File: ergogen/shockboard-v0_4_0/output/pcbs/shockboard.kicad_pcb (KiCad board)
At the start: 2 copper layers, 282.9 x 126 mm, 159 parts

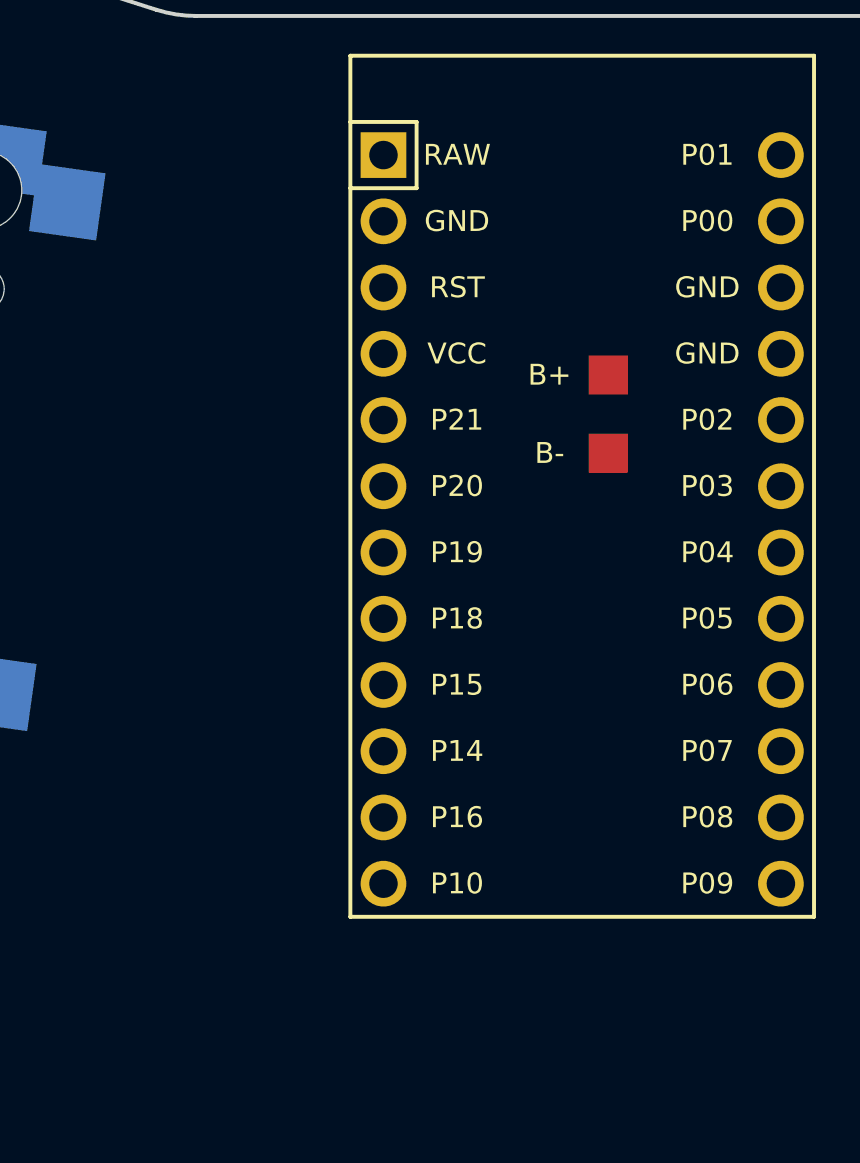
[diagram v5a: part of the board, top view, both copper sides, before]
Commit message: feat: added reset switch and oled
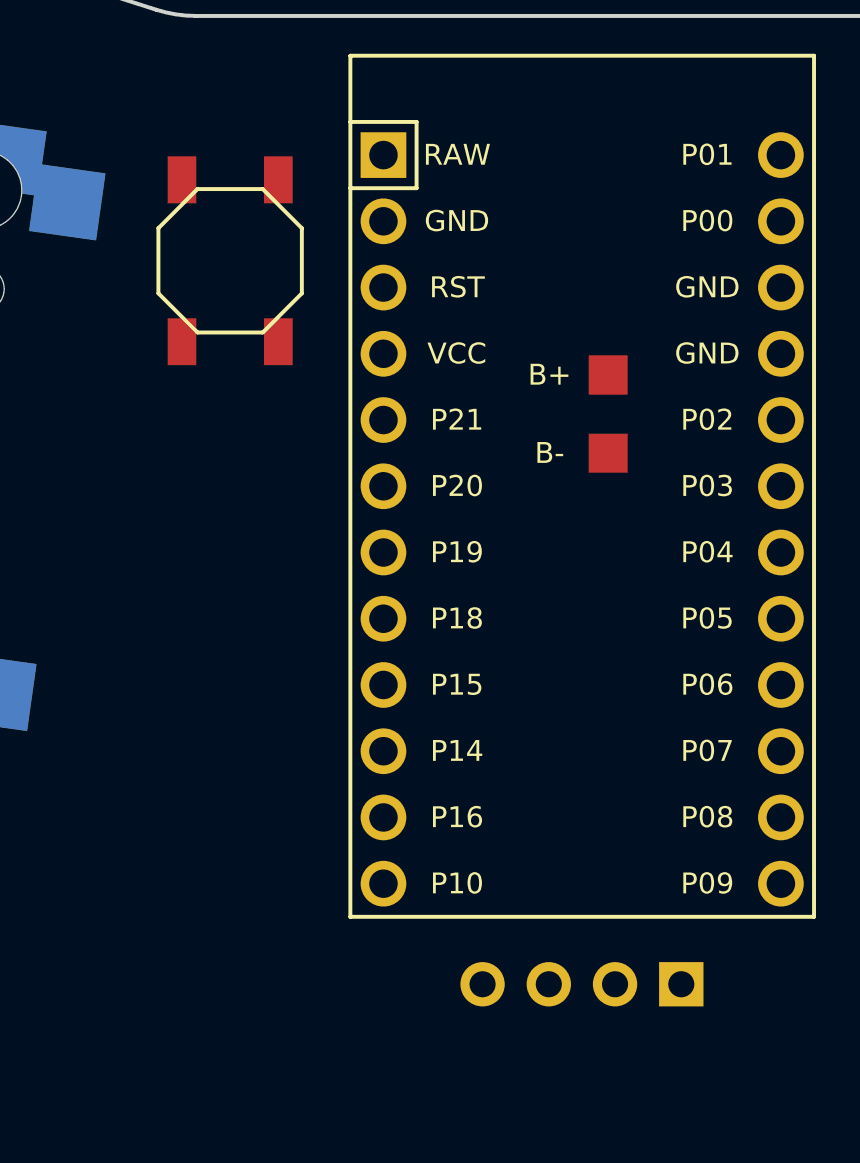
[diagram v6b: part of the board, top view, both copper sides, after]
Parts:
- added B1: , E73:SW_TACT_ALPS_SKQGABE010, F.Cu at (198.9, 92.2)
- added OLED1: OLED, lib:OLED_headers, F.Cu at (206.4, 121.5)
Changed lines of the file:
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@@
 (fp_text user B- (at -2.25 0 0) (layer F.SilkS) (effects (font (size 0.8 0.8) (thickness 0.15)) ))
         )
+        (module lib:OLED_headers (layer F.Cu)
+        (at 206.3782709 121.5245405 90)
+        (fp_text reference "OLED1" (at 0 0) (layer F.SilkS) hide (effects (font (size 1.27 1.27) (thickness 0.15))))
+        (fp_text value OLED (at 0 -7.3) (layer F.Fab) (effects (font (size 1 1) (thickness 0.15))))
+        (pad 4 thru_hole oval (at 1.6 2.18 360) (size 1.7 1.7) (drill 1) (layers *.Cu *.Mask)
+        (net 43 "P2"))
+        (pad 3 thru_hole oval (at 1.6 4.72 360) (size 1.7 1.7) (drill 1) (layers *.Cu *.Mask)
+        (net 48 "P3"))
+        (pad 2 thru_hole oval (at 1.6 7.26 360) (size 1.7 1.7) (drill 1) (layers *.Cu *.Mask)
+        (net 73 "VCC"))
+        (pad 1 thru_hole rect (at 1.6 9.8 360) (size 1.7 1.7) (drill 1) (layers *.Cu *.Mask)
+        (net 71 "GND"))
+        )
+    (module E73:SW_TACT_ALPS_SKQGABE010 (layer F.Cu)
+        (descr "Low-profile SMD Tactile Switch, https://www.e-switch.com/product-catalog/tact/product-lines/tl3342-series-low-profile-smt-tact-switch")
+        (tags "SPST Tactile Switch")
+        (at 198.87827089999996 92.1818495 90)
+        (fp_text reference "B1" (at 0 0) (layer F.SilkS) hide (effects (font (size 1.27 1.27) (thickness 0.15))))
+        (fp_text value "" (at 0 0) (layer F.SilkS) hide (effects (font (size 1.27 1.27) (thickness 0.15))))
+        (fp_line (start 2.75 1.25) (end 1.25 2.75) (layer F.SilkS) (width 0.15))
+        (fp_line (start 2.75 -1.25) (end 1.25 -2.75) (layer F.SilkS) (width 0.15))
+        (fp_line (start 2.75 -1.25) (end 2.75 1.25) (layer F.SilkS) (width 0.15))
+        (fp_line (start -1.25 2.75) (end 1.25 2.75) (layer F.SilkS) (width 0.15))
+        (fp_line (start -1.25 -2.75) (end 1.25 -2.75) (layer F.SilkS) (width 0.15))
+        (fp_line (start -2.75 1.25) (end -1.25 2.75) (layer F.SilkS) (width 0.15))
+        (fp_line (start -2.75 -1.25) (end -1.25 -2.75) (layer F.SilkS) (width 0.15))
+        (fp_line (start -2.75 -1.25) (end -2.75 1.25) (layer F.SilkS) (width 0.15))
+        (pad 1 smd rect (at -3.1 -1.85 90) (size 1.8 1.1) (layers F.Cu F.Paste F.Mask) (net 71 "GND"))
+        (pad 1 smd rect (at 3.1 -1.85 90) (size 1.8 1.1) (layers F.Cu F.Paste F.Mask) (net 71 "GND"))
+        (pad 2 smd rect (at -3.1 1.85 90) (size 1.8 1.1) (layers F.Cu F.Paste F.Mask) (net 72 "RST"))
+        (pad 2 smd rect (at 3.1 1.85 90) (size 1.8 1.1) (layers F.Cu F.Paste F.Mask) (net 72 "RST"))
+    )
             (gr_line (start 281.0227501060654 193.85241200000002) (end 143.73379169393456 193.85241200000002) (angle 90) (layer Edge.Cuts) (width 0.15))
 (gr_line (start 140.8586163541582 192.94305577204256) (end 87.51792705748205 155.4516883672485) (angle 90) (layer Edge.Cuts) (width 0.15))

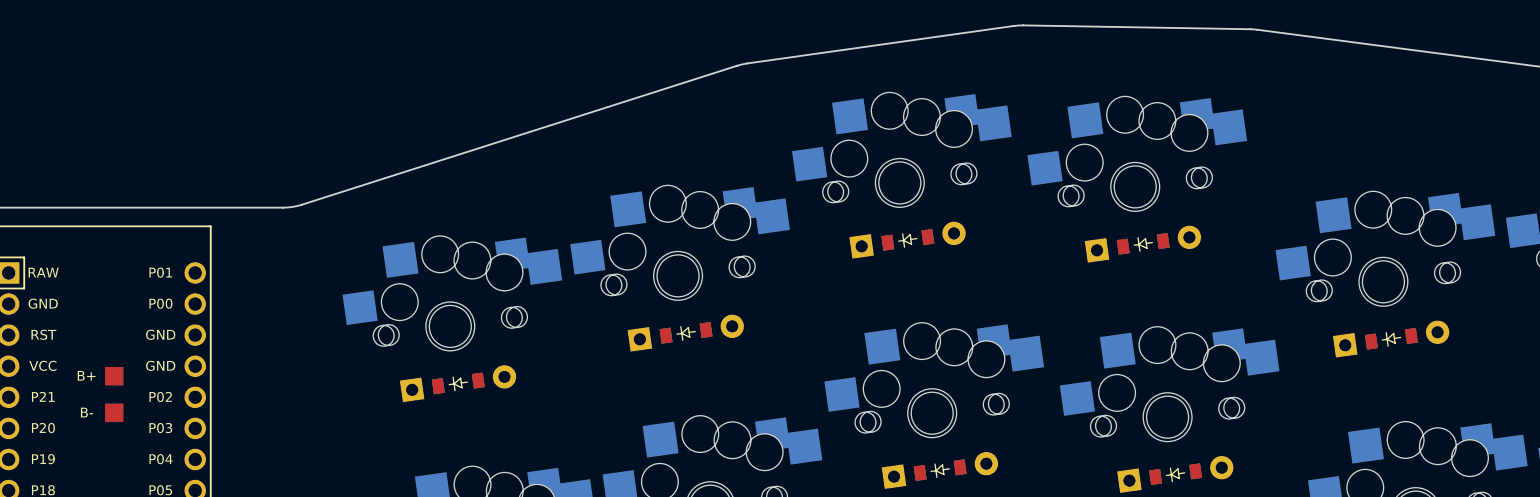
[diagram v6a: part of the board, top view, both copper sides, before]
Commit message: feat: added battery switch
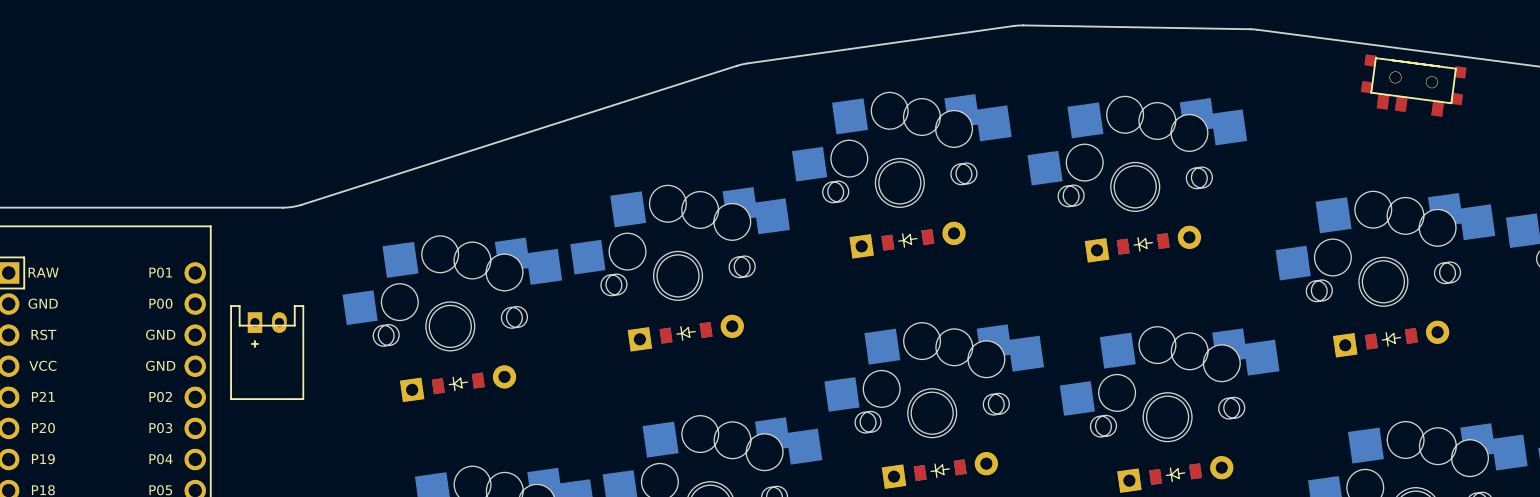
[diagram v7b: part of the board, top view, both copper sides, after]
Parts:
- removed PAD1, PAD2: , SMDPad
- added JST1: , JST_PH_S2B-PH-K_02x2.00mm_Angled, F.Cu at (225.9, 92.2)
- added T1: , E73:SPDT_C128955, F.Cu at (319.6, 72.3)
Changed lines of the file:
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@@
 (net 73 "VCC")
 (net 74 "P10")
+(net 75 "B+")
   (net_class Default "This is the default net class."
     (clearance 0.2)
@@
 (add_net "VCC")
 (add_net "P10")
+(add_net "B+")
   )
       (module MX (layer F.Cu)
@@
         (pad 24 thru_hole circle (at 13.97 -7.62 0) (size 1.7526 1.7526) (drill 1.0922) (layers *.Cu *.SilkS *.Mask) (net 67 "P9"))
       )
-        (module SMDPad (layer F.Cu)
-            (at 213.3782709 96.5615405 0)
-            (fp_text reference "PAD1" (at 0 0) (layer F.SilkS) hide (effects (font (size 1.27 1.27) (thickness 0.15))))
-            (fp_text value "" (at 0 0) (layer F.SilkS) hide (effects (font (size 1.27 1.27) (thickness 0.15))))
-            (pad 1 smd rect (at 0 0 0) (size 1.5 1.5) (layers F.Cu F.Paste F.Mask) (net 70 "RAW"))
-(fp_text user B+ (at -2.25 0 0) (layer F.SilkS) (effects (font (size 0.8 0.8) (thickness 0.15)) ))
-        )
-        (module SMDPad (layer F.Cu)
-            (at 213.3782709 99.5615405 0)
-            (fp_text reference "PAD2" (at 0 0) (layer F.SilkS) hide (effects (font (size 1.27 1.27) (thickness 0.15))))
-            (fp_text value "" (at 0 0) (layer F.SilkS) hide (effects (font (size 1.27 1.27) (thickness 0.15))))
-            (pad 1 smd rect (at 0 0 0) (size 1.5 1.5) (layers F.Cu F.Paste F.Mask) (net 71 "GND"))
-(fp_text user B- (at -2.25 0 0) (layer F.SilkS) (effects (font (size 0.8 0.8) (thickness 0.15)) ))
-        )
         (module lib:OLED_headers (layer F.Cu)
         (at 206.3782709 121.5245405 90)
@@
         (pad 2 smd rect (at 3.1 1.85 90) (size 1.8 1.1) (layers F.Cu F.Paste F.Mask) (net 72 "RST"))
     )
+        (module E73:SPDT_C128955 (layer F.Cu)
+            (at 319.5512817 72.3458067 -7.5)
+            (fp_text reference "T1" (at 0 0) (layer F.SilkS) hide (effects (font (size 1.27 1.27) (thickness 0.15))))
+            (fp_text value "" (at 0 0) (layer F.SilkS) hide (effects (font (size 1.27 1.27) (thickness 0.15))))
+            (fp_line (start 1.95 -1.35) (end -1.95 -1.35) (layer F.SilkS) (width 0.15))
+            (fp_line (start 0 -1.35) (end -3.3 -1.35) (layer F.SilkS) (width 0.15))
+            (fp_line (start -3.3 -1.35) (end -3.3 1.5) (layer F.SilkS) (width 0.15))
+            (fp_line (start -3.3 1.5) (end 3.3 1.5) (layer F.SilkS) (width 0.15))
+            (fp_line (start 3.3 1.5) (end 3.3 -1.35) (layer F.SilkS) (width 0.15))
+            (fp_line (start 0 -1.35) (end 3.3 -1.35) (layer F.SilkS) (width 0.15))
+            (fp_line (start -1.95 -3.85) (end 1.95 -3.85) (layer Dwgs.User) (width 0.15))
+            (fp_line (start 1.95 -3.85) (end 1.95 -1.35) (layer Dwgs.User) (width 0.15))
+            (fp_line (start -1.95 -1.35) (end -1.95 -3.85) (layer Dwgs.User) (width 0.15))
+            (pad "" np_thru_hole circle (at 1.5 0) (size 1 1) (drill 0.9) (layers *.Cu *.Mask))
+            (pad "" np_thru_hole circle (at -1.5 0) (size 1 1) (drill 0.9) (layers *.Cu *.Mask))
+            (pad 1 smd rect (at 2.25 2.075 -7.5) (size 0.9 1.25) (layers F.Cu F.Paste F.Mask) (net 70 "RAW"))
+            (pad 2 smd rect (at -0.75 2.075 -7.5) (size 0.9 1.25) (layers F.Cu F.Paste F.Mask) (net 75 "B+"))
+            (pad 3 smd rect (at -2.25 2.075 -7.5) (size 0.9 1.25) (layers F.Cu F.Paste F.Mask))
+            (pad "" smd rect (at 3.7 -1.1 -7.5) (size 0.9 0.9) (layers F.Cu F.Paste F.Mask))
+            (pad "" smd rect (at 3.7 1.1 -7.5) (size 0.9 0.9) (layers F.Cu F.Paste F.Mask))
+            (pad "" smd rect (at -3.7 1.1 -7.5) (size 0.9 0.9) (layers F.Cu F.Paste F.Mask))
+            (pad "" smd rect (at -3.7 -1.1 -7.5) (size 0.9 0.9) (layers F.Cu F.Paste F.Mask))
+        )
+    (module JST_PH_S2B-PH-K_02x2.00mm_Angled (layer F.Cu)
+        (descr "JST PH series connector, S2B-PH-K, side entry type, through hole, Datasheet: http://www.jst-mfg.com/product/pdf/eng/ePH.pdf")
+        (tags "connector jst ph")
+        (at 225.87827089999996 92.1818495 0)
+        (fp_text reference "JST1" (at 0 0) (layer F.SilkS) hide (effects (font (size 1.27 1.27) (thickness 0.15))))
+        (fp_text value "" (at 0 0) (layer F.SilkS) hide (effects (font (size 1.27 1.27) (thickness 0.15))))
+        (fp_line (start -2.25 0.25) (end -2.25 -1.35) (layer F.SilkS) (width 0.15))
+        (fp_line (start -2.25 -1.35) (end -2.95 -1.35) (layer F.SilkS) (width 0.15))
+        (fp_line (start -2.95 -1.35) (end -2.95 6.25) (layer F.SilkS) (width 0.15))
+        (fp_line (start -2.95 6.25) (end 2.95 6.25) (layer F.SilkS) (width 0.15))
+        (fp_line (start 2.95 6.25) (end 2.95 -1.35) (layer F.SilkS) (width 0.15))
+        (fp_line (start 2.95 -1.35) (end 2.25 -1.35) (layer F.SilkS) (width 0.15))
+        (fp_line (start 2.25 -1.35) (end 2.25 0.25) (layer F.SilkS) (width 0.15))
+        (fp_line (start 2.25 0.25) (end -2.25 0.25) (layer F.SilkS) (width 0.15))
+        (fp_line (start -1 1.5) (end -1 2.0) (layer F.SilkS) (width 0.15))
+        (fp_line (start -1.25 1.75) (end -0.75 1.75) (layer F.SilkS) (width 0.15))
+        (pad 1 thru_hole rect (at -1 0 0) (size 1.2 1.7) (drill 0.75) (layers *.Cu *.Mask) (net 75 "B+"))
+        (pad 2 thru_hole oval (at 1 0 0) (size 1.2 1.7) (drill 0.75) (layers *.Cu *.Mask) (net 71 "GND"))
+    )
             (gr_line (start 281.0227501060654 193.85241200000002) (end 143.73379169393456 193.85241200000002) (angle 90) (layer Edge.Cuts) (width 0.15))

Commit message: wip: mounting holes
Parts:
- added _1: , MountingHole_2.2mm_M2_Pad_Via, F.Cu at (183.9, 92.5)
- added _2: , MountingHole_2.2mm_M2_Pad_Via, F.Cu at (240.8, 92.5)
- added _3: , MountingHole_2.2mm_M2_Pad_Via, F.Cu at (88.9, 86.2)
- added _4: , MountingHole_2.2mm_M2_Pad_Via, F.Cu at (335.9, 86.2)
- added _5: , MountingHole_2.2mm_M2_Pad_Via, F.Cu at (176.0, 148.9)
- added _6: , MountingHole_2.2mm_M2_Pad_Via, F.Cu at (248.8, 148.9)
- added _7: , MountingHole_2.2mm_M2_Pad_Via, F.Cu at (99.7, 145.3)
- added _8: , MountingHole_2.2mm_M2_Pad_Via, F.Cu at (325.0, 145.3)
